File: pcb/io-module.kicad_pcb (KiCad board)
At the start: 4 copper layers, 50 x 25 mm, 127 parts, among them J1 SWD Header, J12 Conn_02x02_Odd_Even, SW1 SKRPABE010, U1 STM32C051G8Ux, Y1 ECS-480-10-37B2-RWN-TR

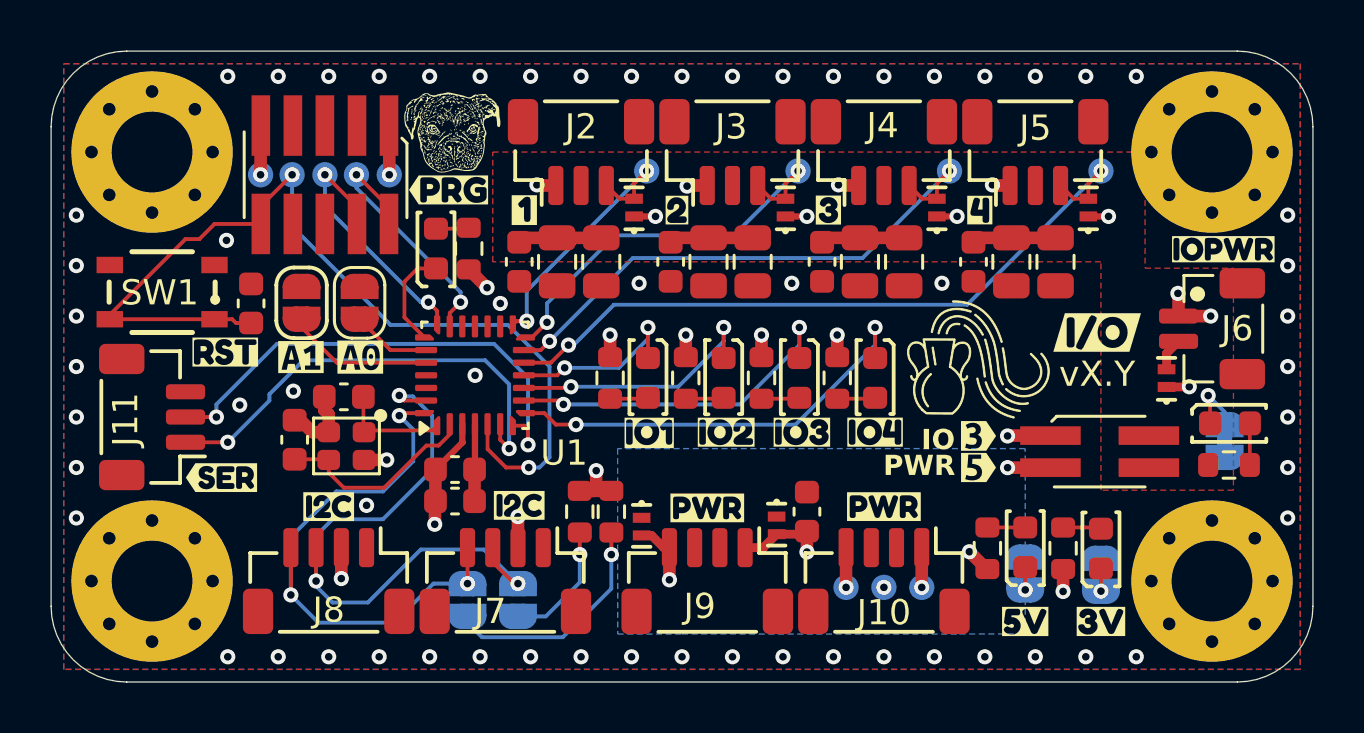
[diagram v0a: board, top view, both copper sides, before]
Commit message: Ran clean up and DRC
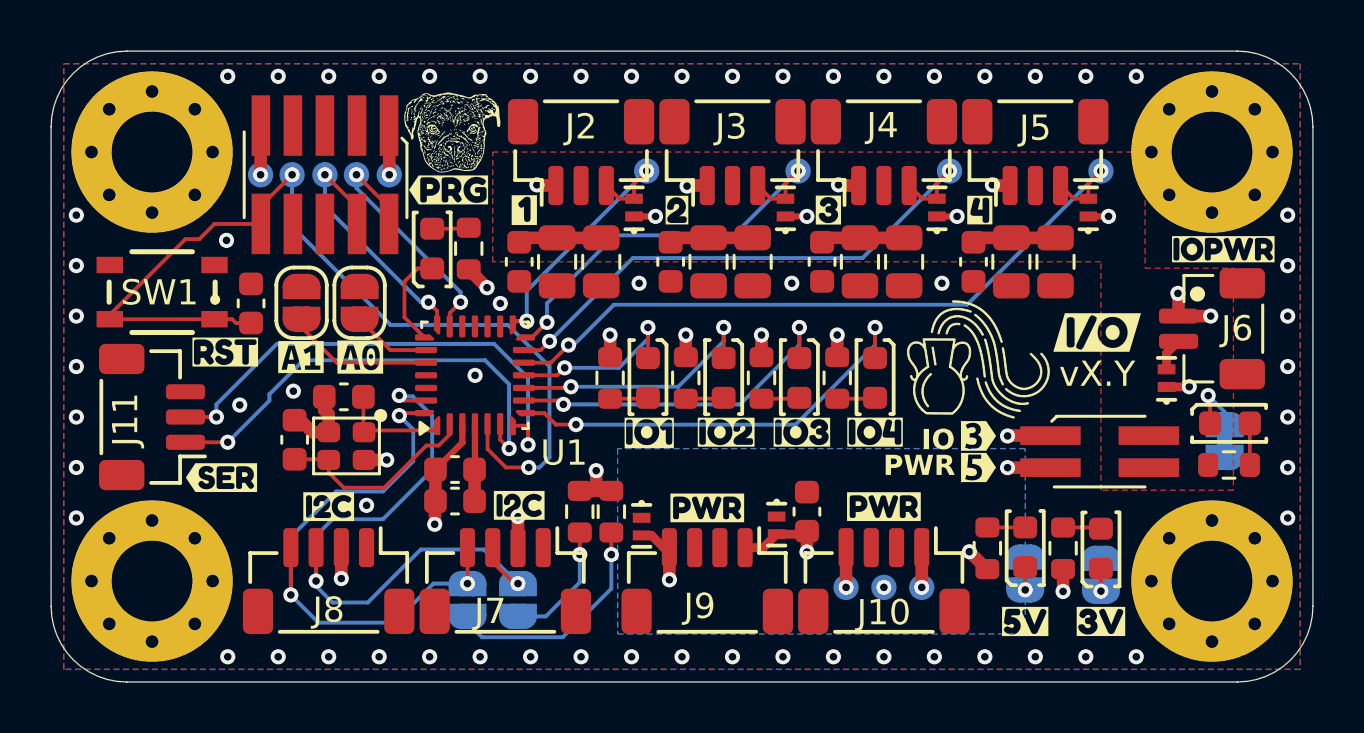
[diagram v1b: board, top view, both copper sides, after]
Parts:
- moved D15 0.15 mm to (65.1, 92.8)
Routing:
- net SDA: track 25.8 -> 25.0 mm
